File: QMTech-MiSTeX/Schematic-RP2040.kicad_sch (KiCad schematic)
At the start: 27 parts, among them J14 Conn_01x05_Pin, J9 Conn_01x02, U1 W25Q128JVS, U2 RP2040, X1 X322512MSB4SI

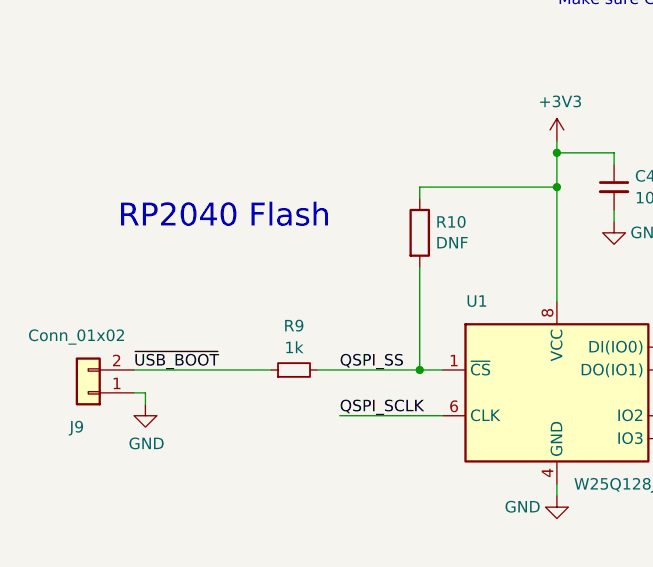
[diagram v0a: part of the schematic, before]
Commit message: add rp2040 vbus, bump rev date, add USB_BOOT connection to RPi
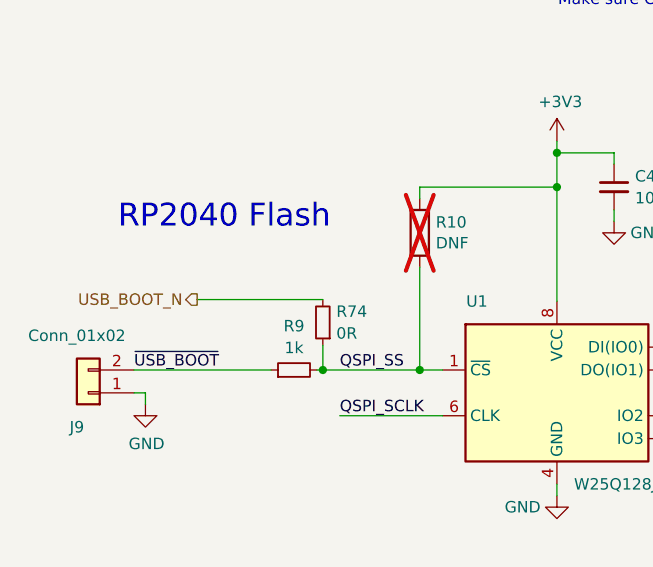
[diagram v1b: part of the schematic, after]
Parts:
- added R74: 0R, R_0603_1608Metric, symbol jlcpcb-basic-resistor-0603:0R
- J14: now left out of the parts list
- R10: now not fitted; now left out of the parts list
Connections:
- net QSPI_SS: now also R74.1
- new net USB_BOOT_N: R74.2
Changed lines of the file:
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@@
 	)
 	(junction
+		(at 46.99 81.4832)
+		(diameter 0)
+		(color 0 0 0 0)
+	)
+	(junction
 		(at 114.0206 28.7782)
 		(diameter 0)
@@
 	(wire
 		(pts
-			(xy 46.3296 81.4832) (xy 57.7596 81.4832)
+			(xy 46.3296 81.4832) (xy 46.99 81.4832)
 		)
 		(stroke
@@
 	(wire
 		(pts
+			(xy 46.99 81.4832) (xy 57.7596 81.4832)
+		)
+		(stroke
+			(width 0)
+			(type default)
+		)
+	)
+	(wire
+		(pts
 			(xy 186.4246 120.2042) (xy 186.4106 120.2182)
 		)
@@
 	(wire
 		(pts
-			(xy 125.4506 37.6503) (xy 125.4506 36.3982)
+			(xy 33.02 73.66) (xy 46.99 73.66)
 		)
 		(stroke
@@
 	(wire
 		(pts
-			(xy 237.2106 22.4282) (xy 237.2106 21.1582)
+			(xy 125.4506 37.6503) (xy 125.4506 36.3982)
 		)
 		(stroke
@@
 	(wire
 		(pts
-			(xy 26.0096 81.4832) (xy 41.2496 81.4832)
+			(xy 237.2106 22.4282) (xy 237.2106 21.1582)
 		)
 		(stroke
@@
 	(wire
 		(pts
+			(xy 26.0096 81.4832) (xy 41.2496 81.4832)
+		)
+		(stroke
+			(width 0)
+			(type default)
+		)
+	)
+	(wire
+		(pts
 			(xy 39.0906 113.3602) (xy 44.1706 113.3602)
 		)
@@
 	(wire
 		(pts
+			(xy 46.99 78.74) (xy 46.99 81.4832)
+		)
+		(stroke
+			(width 0)
+			(type default)
+		)
+	)
+	(wire
+		(pts
 			(xy 72.9996 57.3532) (xy 72.9996 61.1632)
 		)
@@
 		)
 	)
+	(hierarchical_label "USB_BOOT_N"
+		(shape output)
+		(at 33.02 73.66 180)
+		(fields_autoplaced yes)
+		(effects
+			(font
+				(size 1.27 1.27)
+			)
+			(justify right)
+		)
+	)
 	(hierarchical_label "UART0_RX"
 		(shape input)
@@
 		(unit 1)
 		(exclude_from_sim no)
-		(in_bom yes)
+		(in_bom no)
 		(on_board yes)
 		(dnp no)
@@
 		(unit 1)
 		(exclude_from_sim no)
-		(in_bom yes)
+		(in_bom no)
 		(on_board yes)
-		(dnp no)
+		(dnp yes)
 		(property "Reference" "R10"
 			(at 59.5376 65.0748 0)
@@
 					(unit 1)
 				)
+			)
+		)
+	)
+	(symbol
+		(lib_id "jlcpcb-basic-resistor-0603:0R")
+		(at 46.99 76.2 180)
+		(unit 1)
+		(exclude_from_sim no)
+		(in_bom yes)
+		(on_board yes)
+		(dnp no)
+		(fields_autoplaced yes)
+		(property "Reference" "R74"
+			(at 48.4886 74.9879 0)
+			(effects
+				(font
+					(size 1.27 1.27)
+				)
+				(justify right)
+			)
+		)
+		(property "Value" "0R"
+			(at 48.4886 77.4121 0)
+			(effects
+				(font
+					(size 1.27 1.27)
+				)
+				(justify right)
+			)
+		)
+		(property "Footprint" "R_0603_1608Metric"
+			(at 48.768 76.2 90)
+			(effects
+				(font
+					(size 1.27 1.27)
+				)
+				(hide yes)
+			)
+		)
+		(property "Datasheet" "https://datasheet.lcsc.com/szlcsc/Uniroyal-Elec-0603WAF0000T5E_C21189.pdf"
+			(at 46.99 76.2 90)
+			(effects
+				(font
+					(size 1.27 1.27)
+				)
+				(hide yes)
+			)
+		)
+		(property "Description" ""
+			(at 46.99 76.2 0)
+			(effects
+				(font
+					(size 1.27 1.27)
+				)
+				(hide yes)
+			)
+		)
+		(property "LCSC" "C21189"
+			(at 46.99 76.2 90)
+			(effects
+				(font
+					(size 1.27 1.27)
+				)
+				(hide yes)
+			)
+		)
+		(pin "2"
+		)
+		(pin "1"
+		)
+		(instances
+			(project "QMTech-MiSTeX"
+				(path "/bf95850e-2fcb-4784-a603-f17fc357556b/6eb28fc4-fd96-4fb7-b136-67141c56dbda"
+					(reference "R74")
+					(unit 1)
+				)
